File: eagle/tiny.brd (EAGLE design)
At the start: 100 x 80 mm, 29 parts, among them Q3 16MHz, T1 2N3565, T2 2N3565, U1 ATTINY48-MU

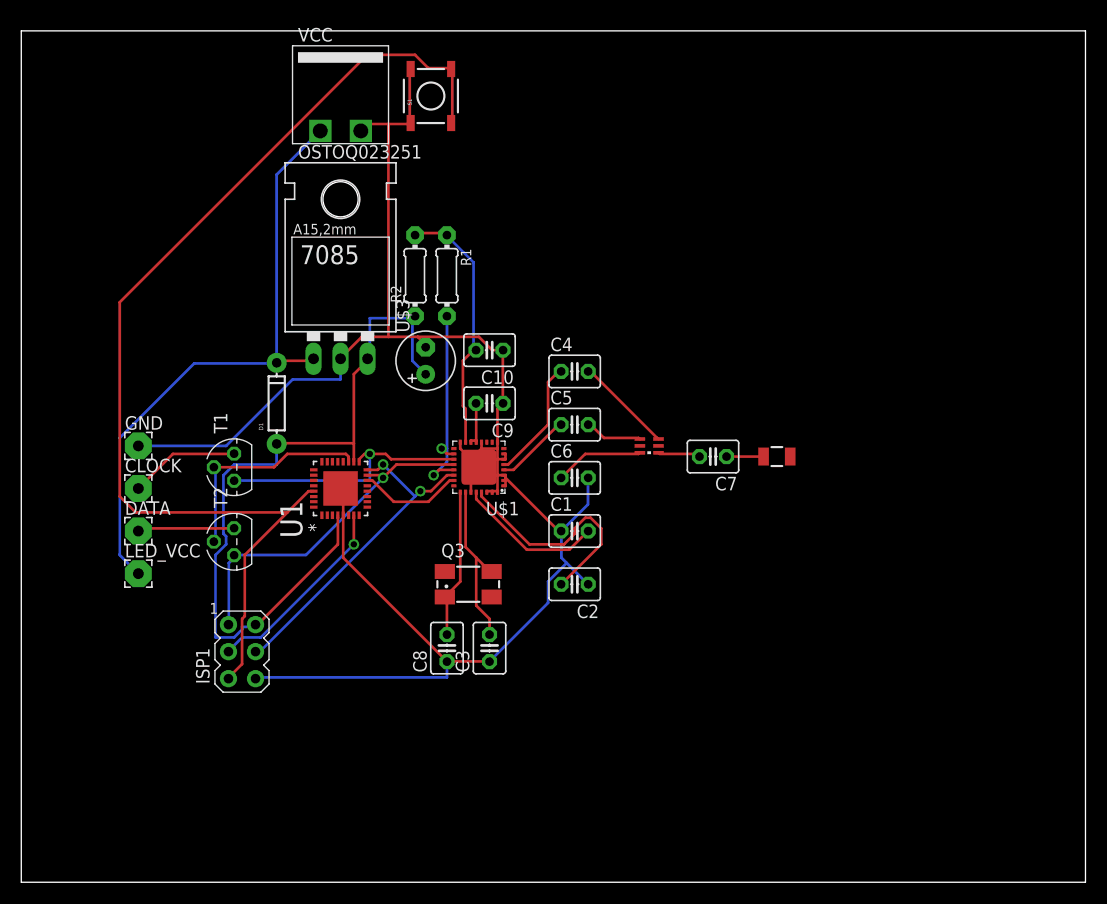
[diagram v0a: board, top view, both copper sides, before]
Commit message: Make a tiny prototype of skylighting
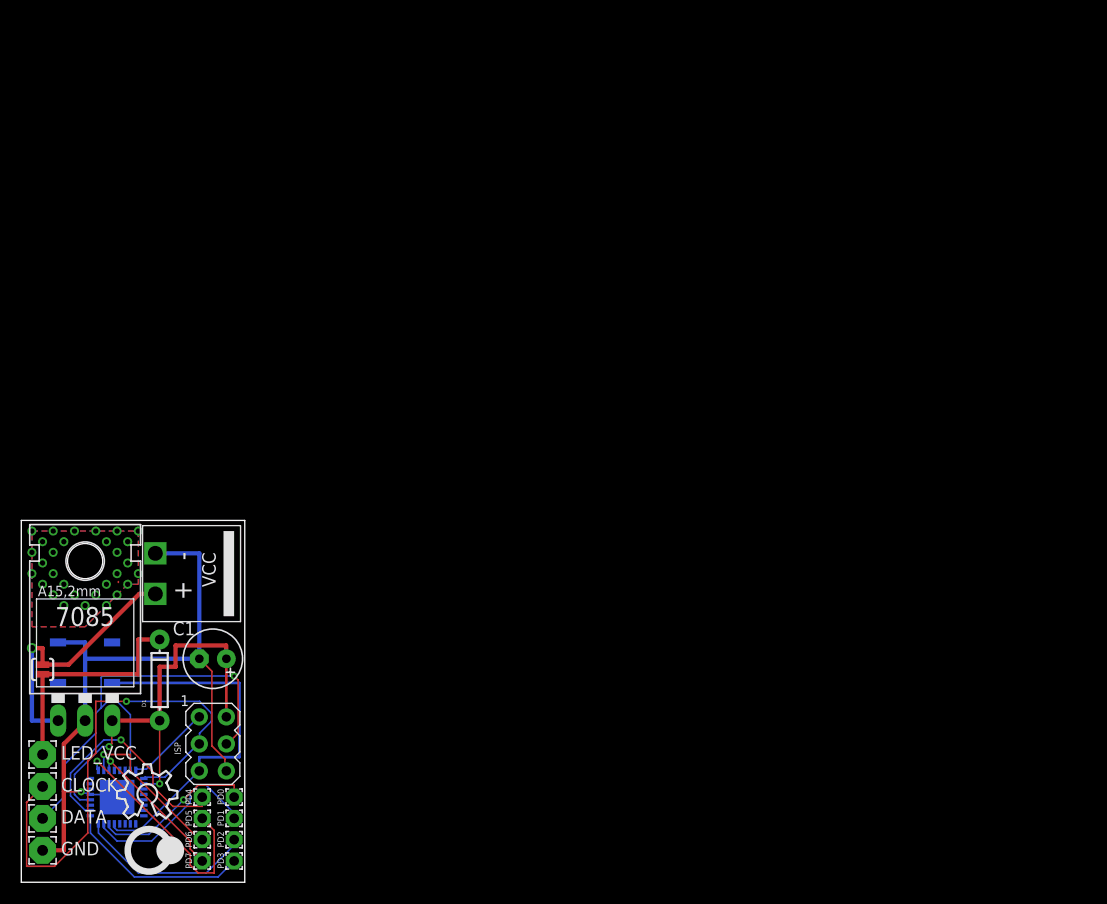
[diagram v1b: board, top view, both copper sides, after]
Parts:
- removed C10, C2, C9: 1uF, adafruit:C025-030X050
- removed C3, C8: 12pF, adafruit:C025-030X050
- removed C4, C5, C6: 22pF, adafruit:C025-030X050
- removed C7: 1.5pF, adafruit:C025-030X050
- removed F1: 2450BM15A0002, johanson-technology:2450BM15A0002
- removed Q3: 16MHz, adafruit:CTS406
- removed R1: 220, adafruit:0204/7
- removed R2: 123.75, adafruit:0204/7
- removed T1, T2: 2N3565, transistor:TO92
- removed U$3: (no value), adafruit:E2,5-6
- removed U$4: ANTENNA2SMD, SparkFun:ANTENNA-CHIP2
- added PD0, PD1, PD2, PD3, PD4, PD5, PD6, PD7: (no value), wirepad:1,6/0,9
- added SJ1: LED_VCC = VCC, SparkFun:SJ_2S-NO
- added U$2: (no value), ohw-logo:OSHW_8X200_NOTEXT
- C1: value 1uF -> (none); device adafruit:C025-030X050 -> adafruit:E2,5-6
- U$1: value AT86RF231 -> (none); device at86rf231:QFN32 -> phrobo:PHROBO-LOGO
- moved S1 62.4 mm to (5.99, 20.6), flipped to the bottom, turned to 0 degrees
- moved U$1 47.5 mm to (12.0, 3.00), turned to 0 degrees
- moved VCC 47.1 mm to (16.0, 29.0), turned to 270 degrees
- moved 7085 41.6 mm to (6.00, 19.0)
- moved GND 39.1 mm to (2.00, 3.00)
- moved C1 36.1 mm to (18.0, 21.0), turned to 180 degrees
- moved U1 35.8 mm to (9.00, 8.00), flipped to the bottom, turned to 180 degrees
- moved CLOCK 29.4 mm to (2.00, 9.00)
- moved DATA 28.5 mm to (2.00, 6.00)
- moved D1 28.2 mm to (13.0, 19.0)
- moved LED_VCC 19.2 mm to (2.00, 12.0)
- moved ISP1 9.09 mm to (18.0, 13.0)
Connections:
- removed net AVDD: C2.2, U$1.29
- removed net DEVDD: C10.2, R1.1, R2.2, U$1.15
- removed net DVDD2: C9.2, U$1.13, U$1.14
- removed net EVDD: C1.2, U$1.28
- removed net N$1: T1.2, T2.2, U1.19
- removed net N$10: C5.2, F1.4
- removed net N$11: T1.3, U$1.19, U1.17
- removed net N$12: DATA.1, T2.1
- removed net N$13: ISP1.3, U1.7
- removed net N$14: C4.1, U$1.5
- removed net N$15: C8.2, Q3.1, U$1.25
- removed net N$16: C3.2, Q3.3, U$1.26
- removed net N$17: R1.2, U$1.18, U$1.21
- removed net N$18: C7.2, F1.1
- removed net N$2: C5.1, U$1.4
- removed net N$23: C6.1, F1.6
- removed net N$24: C7.1, U$4.FEED
- removed net N$3: ISP1.4, U$1.22, U1.16
- removed net N$5: CLOCK.1, T1.1
- removed net N$8: C4.2, F1.3
- removed net N$9: U$1.23, U1.14
- new net MISO: ISP1.1, U1.16
- new net N$32: PD0.1, U1.30
- new net N$33: PD1.1, U1.31
- new net N$34: PD2.1, U1.32
- new net N$35: PD3.1, U1.1
- new net N$36: PD4.1, U1.2
- new net N$37: PD5.1, U1.9
- new net N$38: PD6.1, U1.10
- new net N$39: PD7.1, U1.11
- new net N$40: D1.C, LED_VCC.1, SJ1.2
- new net SCK: CLOCK.1, ISP1.3, U1.17
- net GND: now also C1.-, U1.21, VCC.P$2; no longer C1.1, C10.1, C2.1, C3.1, C6.2, C8.1, C9.1, S1.1, U$1.1, U$1.12, U$1.16, U$1.2, U$1.27, U$1.3, U$1.30, U$1.31, U$1.32, U$1.6, U$1.7, U$1.9, U$1.EXP, U$3.-, VCC.P$1
- net MOSI: now also DATA.1, ISP1.4; no longer ISP1.1, T2.3, U$1.20
- net N$4: no longer S1.4
- net N$6: now also SJ1.1, VCC.P$1; no longer D1.C, LED_VCC.1, VCC.P$2
- net VCC: now also C1.+; no longer R2.1, U$3.+
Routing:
- net GND: track 174.7 -> 69.1 mm, vias 0 -> 1
- net N$4: track 102.3 -> 34.8 mm
- net SCK: track 0.00 -> 49.1 mm, vias 0 -> 1
- net N$6: track 58.4 -> 25.6 mm, vias 0 -> 1
- net N$3: track 31.6 -> 0.00 mm, vias 2 -> 1
- net VCC: track 73.2 -> 42.4 mm, vias 0 -> 2
- net DEVDD: track 24.9 -> 0.00 mm
- net N$11: track 24.8 -> 0.00 mm, vias 1 -> 0
- net N$36: track 0.00 -> 22.5 mm, vias 0 -> 1
- net N$37: track 0.00 -> 22.4 mm, vias 0 -> 1
- net AVDD: track 22.1 -> 0.00 mm
- net N$40: track 0.00 -> 21.8 mm
- net N$1: track 21.1 -> 0.00 mm, vias 0 -> 1
- net N$17: track 19.4 -> 0.00 mm, vias 2 -> 0
- net N$13: track 18.7 -> 0.00 mm
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- added copper zone on layer 16, net N$29
- added copper zone on layer 1, net N$30
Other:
- board size 100 x 80 mm -> 21 x 34 mm
- board text added: "+"
- board text added: "-"
- board text added: "ISP"
- board text added: "Made At Noisebridge"
- board text added: "Skylighting R3"
